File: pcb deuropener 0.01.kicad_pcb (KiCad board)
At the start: 2 copper layers, 54.6 x 86.4 mm, 31 parts, among them J1 Conn_01x02, J10 Conn_01x03, J11 Barrel_Jack_Switch, J12 Conn_01x08, J13 Conn_01x02, J14 Conn_01x02, J2 Conn_01x02, J3 Conn_01x02, J4 Conn_01x02, J8 Conn_01x02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

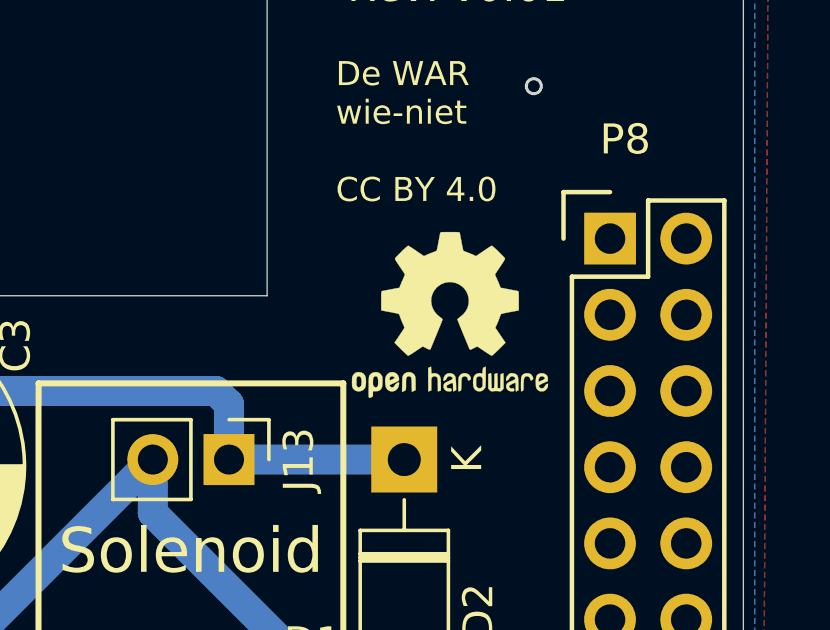
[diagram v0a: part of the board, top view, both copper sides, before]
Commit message: Fixed: 12V barreljack connected to wrong pin #1
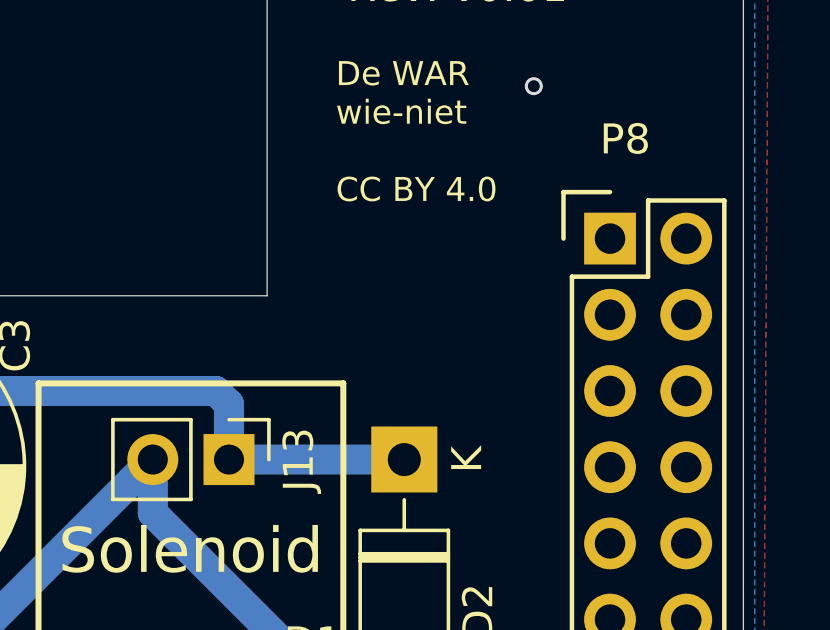
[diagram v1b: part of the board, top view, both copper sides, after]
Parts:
- removed REF**: OSHW-Logo2_7.3x6mm_SilkScreen, Symbol:OSHW-Logo2_7.3x6mm_SilkScreen
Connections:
- J11 pad 2: (no net) -> Earth
- J11 pad 3: Earth -> (no net)

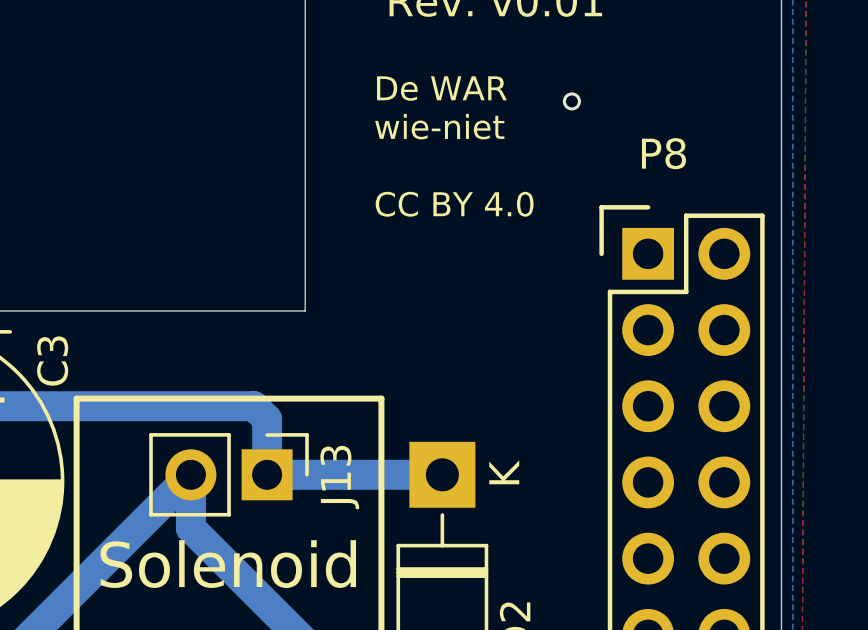
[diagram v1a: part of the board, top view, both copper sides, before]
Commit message: OSHW Logo was removec after last change, re-added (Place >> Footprint >> "search OSHW" and place the smalles logo on print).
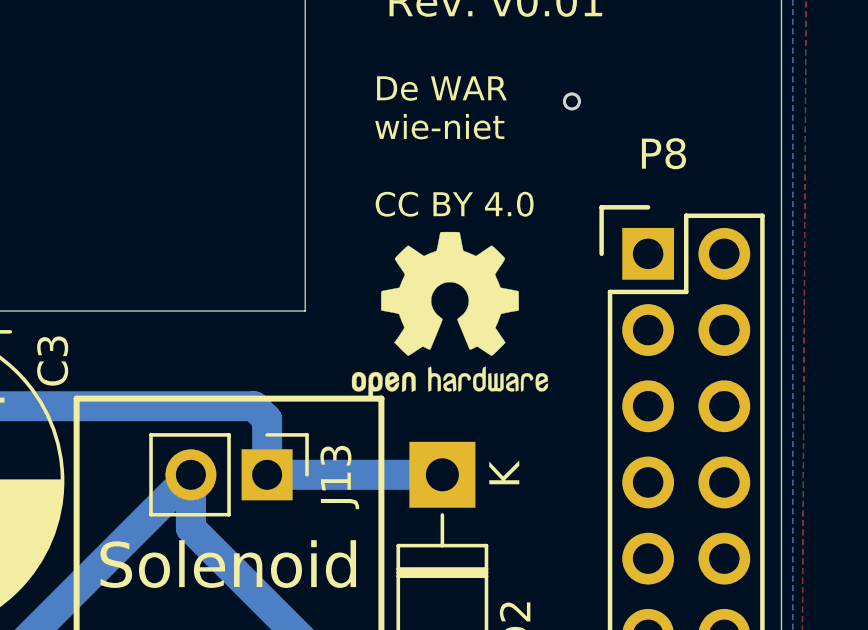
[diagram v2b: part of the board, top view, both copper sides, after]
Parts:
- added REF**: OSHW-Logo2_7.3x6mm_SilkScreen, Symbol:OSHW-Logo2_7.3x6mm_SilkScreen, F.Cu at (158.0, 64.4)
